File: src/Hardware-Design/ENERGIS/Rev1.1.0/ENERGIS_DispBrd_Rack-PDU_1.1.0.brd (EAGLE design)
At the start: 124 x 28 mm, 85 parts, among them CON1 DNI, CON2 AFC11-S20ICC-00, IC1 MCP23017T-E/ML, IC2 MCP23017T-E/ML, T1 DNI

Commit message: general update for the repo
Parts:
- removed U$6, U$7: DNI, ds_silkscreen:NEXTPCB_SMALL
- R4: value DNI -> 10K 1%
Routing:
- net GND: vias 238 -> 243

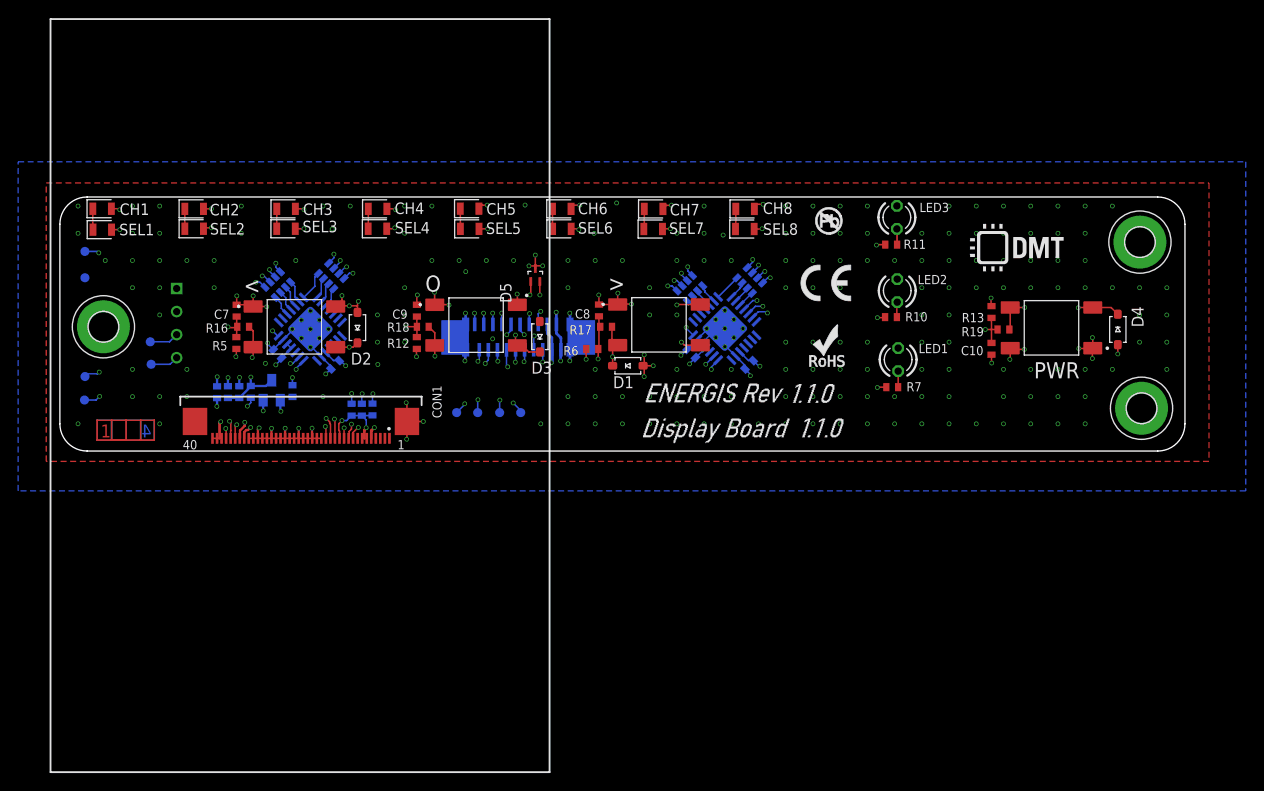
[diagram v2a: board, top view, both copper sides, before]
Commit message: add mac calculation
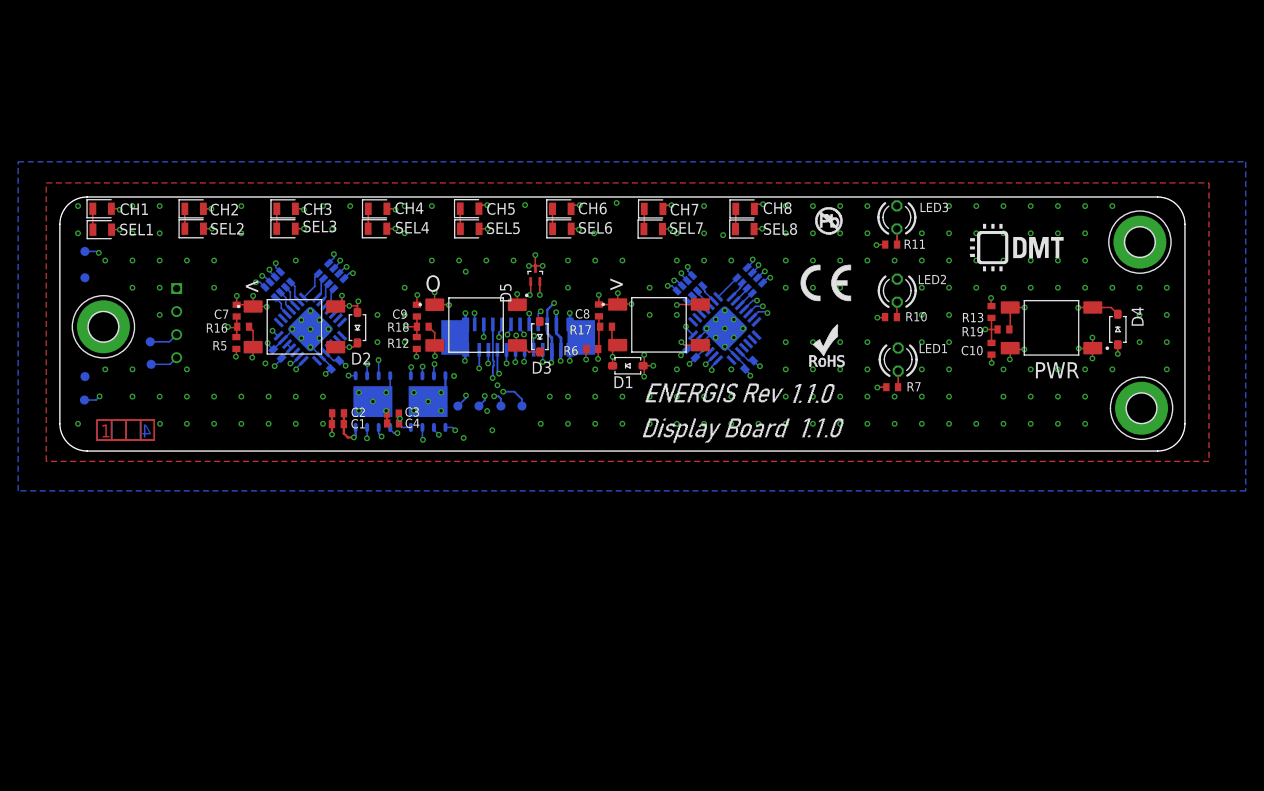
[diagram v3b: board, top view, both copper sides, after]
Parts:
- removed CON1: DNI, ds_con:FPC40_3.5TFT
- removed R1, R2, R3: DNI, ds_passive:0402
- removed R4: 10K 1%, ds_resistor:0402
- removed T1: DNI, ds_active:SOT23
- added IC3, IC4: W25Q128JVPIQ, ds_ic_memory:SON127P600X500X75-8N
- C1, C2: value DNI -> 100nF 25V; device ds_passive:C0402 -> ds_capacitors:0402
- C3, C4: value DNI -> 1uF 16V; device ds_passive:C0402 -> ds_capacitors:0402
- moved C1 13.5 mm to (34.7, 28.2), flipped to the top, turned to 180 degrees
- moved C3 4.57 mm to (40.7, 28.1), flipped to the top, turned to 180 degrees
- moved C2 4.14 mm to (34.6, 27.0), flipped to the top, turned to 180 degrees
- moved C4 3.77 mm to (40.7, 27.0), flipped to the top, turned to 180 degrees
- moved CS 0.73 mm to (47.9, 29.0)
- moved MISO 0.73 mm to (54.9, 29.0)
- moved MOSI 0.73 mm to (52.6, 29.0)
- moved SCK 0.73 mm to (50.2, 29.0)
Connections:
- removed net LCD_CS: CON1.9, CON2.19, CS.TP
- removed net LCD_DC: CON1.10, CON2.18
- removed net LCD_MISO: CON1.14, CON2.15, MISO.TP
- removed net LCD_MOSI: CON1.13, CON2.16, MOSI.TP
- removed net LCD_RES: CON1.15, CON2.14
- removed net LCD_SCLK: CON1.11, CON2.17, SCK.TP
- removed net N$2: CON1.35, R2.2
- removed net N$3: CON1.36, R3.2
- removed net N$4: R1.1, R2.1, R3.1, T1.3
- removed net N$5: CON1.34, R1.2
- new net GPIO_I1/CS2: CON2.13, IC4.1
- new net GPIO_I2/IO3: CON2.14, IC3.7, IC4.7
- new net GPIO_I3/IO2: CON2.18, IC3.3, IC4.3
- new net SPI1_CS: CON2.19, CS.TP, IC3.1
- new net SPI1_MISO/IO1: CON2.15, IC3.2, IC4.2, MISO.TP
- new net SPI1_MOSI/IO0: CON2.16, IC3.5, IC4.5, MOSI.TP
- new net SPI1_SCLK: CON2.17, IC3.6, IC4.6, SCK.TP
- net +3V3: now also IC3.8, IC4.8; no longer CON1.12, CON1.38, CON1.39, CON1.40, CON1.6, CON1.7
- net +5V: no longer CON1.33
- net GND: now also IC3.4, IC3.PAD, IC4.4, IC4.PAD; no longer CON1.16, CON1.17, CON1.18, CON1.19, CON1.20, CON1.21, CON1.22, CON1.23, CON1.24, CON1.25, CON1.26, CON1.27, CON1.28, CON1.29, CON1.30, CON1.31, CON1.32, CON1.37, CON1.5, CON1.Z1, CON1.Z2, R4.2, T1.2
- net LCD_BL: no longer CON2.13, R4.1, T1.1
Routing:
- net LCD_BL: track 63.4 -> 0.00 mm, vias 3 -> 0
- net LCD_MOSI: track 42.1 -> 0.00 mm, vias 4 -> 0
- net LCD_MISO: track 36.9 -> 0.00 mm, vias 3 -> 0
- net LCD_RES: track 34.9 -> 0.00 mm, vias 2 -> 0
- net LCD_SCLK: track 30.3 -> 0.00 mm, vias 3 -> 0
- net GPIO_I2/IO3: track 0.00 -> 30.0 mm, vias 0 -> 3
- net LCD_CS: track 27.7 -> 0.00 mm, vias 3 -> 0
- net LCD_DC: track 27.5 -> 0.00 mm, vias 2 -> 0
- net SPI1_MISO/IO1: track 0.00 -> 27.3 mm, vias 0 -> 4
- net SPI1_MOSI/IO0: track 0.00 -> 26.3 mm, vias 0 -> 4
- net +5V: track 88.2 -> 63.2 mm
- net SPI1_SCLK: track 0.00 -> 23.8 mm, vias 0 -> 4
- net SPI1_CS: track 0.00 -> 21.8 mm, vias 0 -> 3
- net GPIO_I3/IO2: track 0.00 -> 19.4 mm, vias 0 -> 3
- net GPIO_I1/CS2: track 0.00 -> 15.8 mm, vias 0 -> 4
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
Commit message: update documentation
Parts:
- removed IC3, IC4: W25Q128JVPIQ, ds_ic_memory:SON127P600X500X75-8N
- added CON1: DNI, ds_con:FPC40_3.5TFT
- added R1, R2, R3: DNI, ds_passive:0402
- added R4: 10K 1%, ds_resistor:0402
- added T1: DNI, ds_active:SOT23
- C1, C2: value 100nF 25V -> DNI; device ds_capacitors:0402 -> ds_passive:C0402
- C3, C4: value 1uF 16V -> DNI; device ds_capacitors:0402 -> ds_passive:C0402
- R12, R13, R5, R6: value 33K 1% -> 10K 1%
- R16, R17, R18, R19: value 10K 1% -> 0R 1%
- moved C1 13.5 mm to (21.3, 30.5), flipped to the bottom, turned to 270 degrees
- moved C3 4.57 mm to (36.1, 28.6), flipped to the bottom, turned to 90 degrees
- moved C2 4.14 mm to (38.5, 28.6), flipped to the bottom, turned to 90 degrees
- moved C4 3.77 mm to (37.3, 28.6), flipped to the bottom, turned to 90 degrees
- moved CS 0.73 mm to (47.7, 28.2)
- moved MISO 0.73 mm to (54.8, 28.2)
- moved MOSI 0.73 mm to (52.5, 28.2)
- moved SCK 0.73 mm to (50.0, 28.2)
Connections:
- removed net GPIO_I1/CS2: CON2.13, IC4.1
- removed net GPIO_I2/IO3: CON2.14, IC3.7, IC4.7
- removed net GPIO_I3/IO2: CON2.18, IC3.3, IC4.3
- removed net SPI1_CS: CON2.19, CS.TP, IC3.1
- removed net SPI1_MISO/IO1: CON2.15, IC3.2, IC4.2, MISO.TP
- removed net SPI1_MOSI/IO0: CON2.16, IC3.5, IC4.5, MOSI.TP
- removed net SPI1_SCLK: CON2.17, IC3.6, IC4.6, SCK.TP
- new net LCD_CS: CON1.9, CON2.19, CS.TP
- new net LCD_DC: CON1.10, CON2.18
- new net LCD_MISO: CON1.14, CON2.15, MISO.TP
- new net LCD_MOSI: CON1.13, CON2.16, MOSI.TP
- new net LCD_RES: CON1.15, CON2.14
- new net LCD_SCLK: CON1.11, CON2.17, SCK.TP
- new net N$2: CON1.35, R2.2
- new net N$3: CON1.36, R3.2
- new net N$4: R1.1, R2.1, R3.1, T1.3
- new net N$5: CON1.34, R1.2
- net +3V3: now also CON1.12, CON1.38, CON1.39, CON1.40, CON1.6, CON1.7; no longer IC3.8, IC4.8
- net +5V: now also CON1.33
- net GND: now also CON1.16, CON1.17, CON1.18, CON1.19, CON1.20, CON1.21, CON1.22, CON1.23, CON1.24, CON1.25, CON1.26, CON1.27, CON1.28, CON1.29, CON1.30, CON1.31, CON1.32, CON1.37, CON1.5, CON1.Z1, CON1.Z2, R4.2, T1.2; no longer IC3.4, IC3.PAD, IC4.4, IC4.PAD
- net LCD_BL: now also CON2.13, R4.1, T1.1
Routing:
- net LCD_BL: track 0.00 -> 63.4 mm, vias 0 -> 3
- net LCD_MOSI: track 0.00 -> 42.1 mm, vias 0 -> 4
- net LCD_MISO: track 0.00 -> 36.9 mm, vias 0 -> 3
- net LCD_RES: track 0.00 -> 34.9 mm, vias 0 -> 2
- net LCD_SCLK: track 0.00 -> 30.3 mm, vias 0 -> 3
- net GPIO_I2/IO3: track 30.0 -> 0.00 mm, vias 3 -> 0
- net LCD_CS: track 0.00 -> 27.7 mm, vias 0 -> 3
- net LCD_DC: track 0.00 -> 27.5 mm, vias 0 -> 2
- net SPI1_MISO/IO1: track 27.3 -> 0.00 mm, vias 4 -> 0
- net SPI1_MOSI/IO0: track 26.3 -> 0.00 mm, vias 4 -> 0
- net +5V: track 63.2 -> 88.2 mm
- net SPI1_SCLK: track 23.8 -> 0.00 mm, vias 4 -> 0
- net SPI1_CS: track 21.8 -> 0.00 mm, vias 3 -> 0
- net GPIO_I3/IO2: track 19.4 -> 0.00 mm, vias 3 -> 0
- net GPIO_I1/CS2: track 15.8 -> 0.00 mm, vias 4 -> 0
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
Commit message: clear documentation, software bugfix
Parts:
- R4: value 10K 1% -> DNI
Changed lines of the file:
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@@
 <attribute name="VALUE" x="76.388421875" y="32.112653125" size="1.27" layer="28" rot="MR45"/>
 </element>
-<element name="R4" library="ds_resistor" package="0402" package3d_urn="urn:adsk.eagle:package:46683744/3" value="10K 1%" x="29.64" y="30.61" smashed="yes" rot="MR90">
+<element name="R4" library="ds_resistor" package="0402" package3d_urn="urn:adsk.eagle:package:46683744/3" value="DNI" x="29.64" y="30.61" smashed="yes" rot="MR90">
 <attribute name="DESCRIPTION" value="62.5mW Thick Film Resistors 50V ±100ppm/℃ ±1% 10kΩ 0402 Chip Resistor - Surface Mount ROHS" x="29.64" y="30.61" size="1.778" layer="28" rot="MR90" display="off"/>
 <attribute name="HQ_PART" value="RE0207399" x="29.64" y="30.61" size="1.778" layer="28" rot="MR90" display="off"/>
